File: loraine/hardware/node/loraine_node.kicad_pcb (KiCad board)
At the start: 2 copper layers, 50 x 50 mm, 45 parts, among them CON1 BARREL_JACK, IC1 ATTINY2313A-S, K1 LED1, K2 LED2, K3 LED3, P1 POWER_THRU, P2 POWER, P3 SOLDER_PAD, P4 BUS, P5 BUS_THRU, P6 ICSP, P7 OUTPUTS, Q1 TSM3460CX6, Q2 TSM3460CX6, Q3 TSM3460CX6, Q4 TSM3460CX6, Q5 TSM3460CX6, Q6 TSM3460CX6, Q7 TSM3460CX6, Q8 TSM3460CX6, U1 UA7805CKCT, U2 SN65176BD, X1 16MHz

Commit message: Finished both PCBs apart from logos and checking
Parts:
- C1, C2: value 16p -> 16pF
- C4, C6: value 0.1u -> 0.1uF
- moved P6 45.3 mm to (108.6, 130.7)
- moved C6 15.6 mm to (126.2, 115.6), turned to 0 degrees
- moved C4 8.89 mm to (110.5, 136.4), turned to 270 degrees
- moved K2 6.15 mm to (144.4, 105.0)
- moved P7 2.61 mm to (144.9, 128.9)
- moved U1 2.54 mm to (105.4, 122.6)
- moved U2 2.37 mm to (104.4, 137.2), turned to 270 degrees
- moved C3 2.29 mm to (109.0, 125.0)
- moved C5 2.29 mm to (109.0, 120.1)
- moved R9 1.35 mm to (144.4, 146.4)
- moved R1 1.35 mm to (146.9, 146.4)
- moved Q1 1.09 mm to (145.7, 142.2), turned to 180 degrees
- moved C2 0.65 mm to (120.7, 132.8), turned to 0 degrees
- moved X1 0.46 mm to (118.4, 136.9)
- moved C1 0.18 mm to (116.3, 132.8), turned to 180 degrees
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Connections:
- C3 pad 1: +12V -> VIN
- CON1 pad 1: +12V -> VIN
- K1 pad 3: +5V -> VIN
- K2 pad 3: +5V -> VIN
- K3 pad 3: +5V -> VIN
- P1 pad 2: +12V -> VIN
- P2 pad 2: +12V -> VIN
- P3 pad 2: +12V -> VIN
- P7 pad 1: +12V -> VIN
- P7 pad 11: +12V -> VIN
- P7 pad 13: +12V -> VIN
- P7 pad 15: +12V -> VIN
- P7 pad 3: +12V -> VIN
- P7 pad 5: +12V -> VIN
- P7 pad 7: +12V -> VIN
- P7 pad 9: +12V -> VIN
- U1 pad 2: +12V -> VIN
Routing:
- net GND: track 0.00 -> 302.1 mm, vias 0 -> 14
- net VIN: track 0.00 -> 176.9 mm
- net Net-(IC1-Pad13): track 0.00 -> 128.9 mm, vias 0 -> 3
- net +5V: track 0.00 -> 60.8 mm, vias 0 -> 2
- net Net-(IC1-Pad14): track 0.00 -> 55.0 mm, vias 0 -> 2
- net Net-(IC1-Pad12): track 0.00 -> 49.4 mm, vias 0 -> 1
- net /SCK: track 0.00 -> 43.5 mm, vias 0 -> 1
- net Net-(IC1-Pad2): track 0.00 -> 37.4 mm, vias 0 -> 2
- net /MISO: track 0.00 -> 36.5 mm, vias 0 -> 1
- net /MOSI: track 0.00 -> 30.7 mm, vias 0 -> 1
- net Net-(P4-Pad2): track 0.00 -> 23.6 mm
- net Net-(C2-Pad1): track 0.00 -> 17.9 mm
- net Net-(IC1-Pad15): track 0.00 -> 17.8 mm
- net /RESET: track 0.00 -> 17.7 mm
- net Net-(C1-Pad1): track 0.00 -> 17.6 mm
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- added copper zone on B.Cu, net GND
- added copper zone on F.Cu, net GND

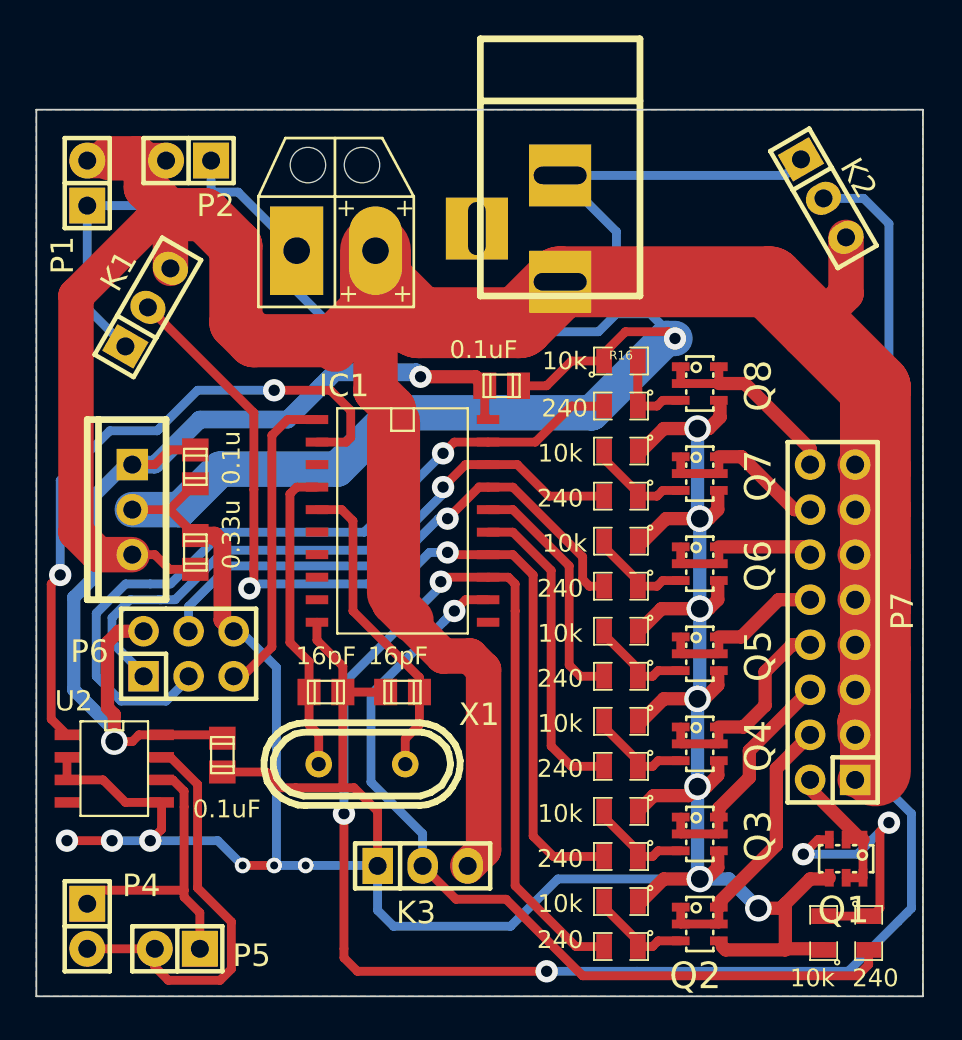
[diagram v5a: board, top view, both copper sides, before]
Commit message: 5V power conn on uplighter board
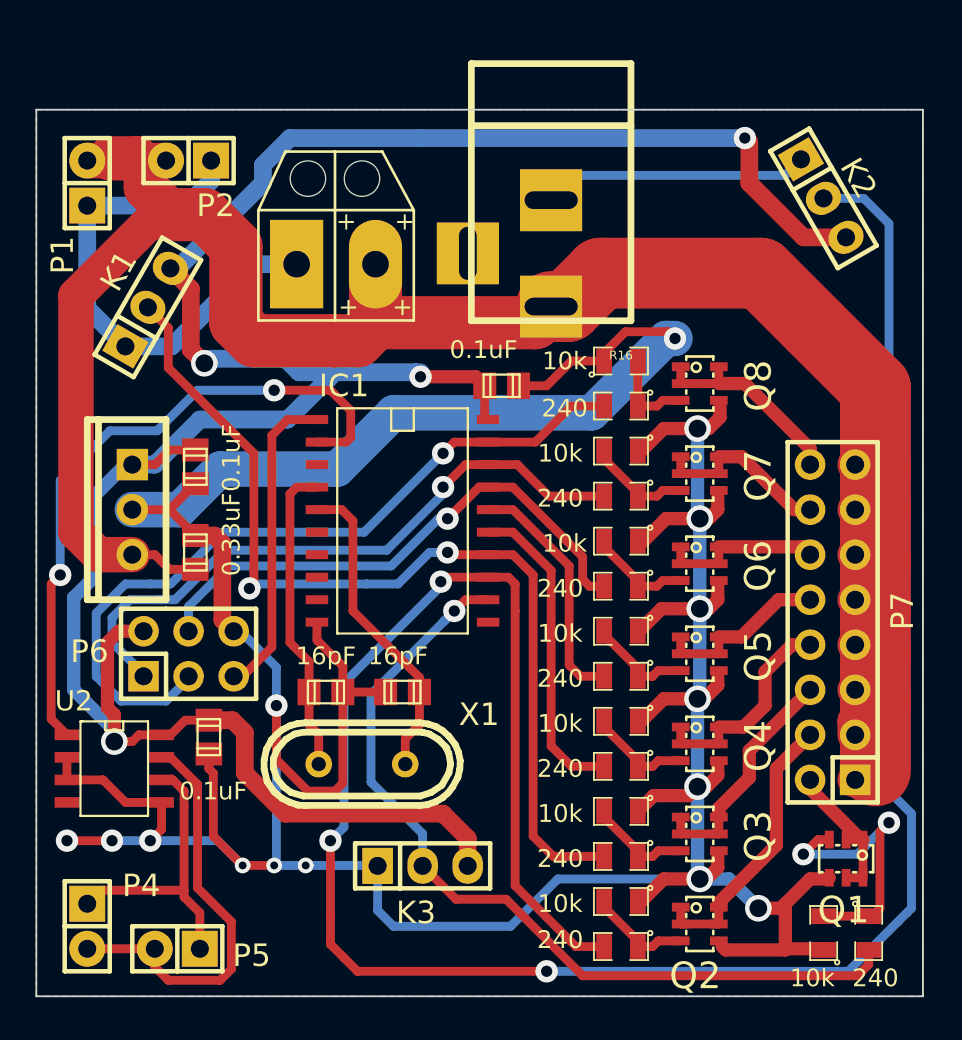
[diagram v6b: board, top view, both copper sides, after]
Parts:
- C3: value 0.33u -> 0.33uF
- C5: value 0.1u -> 0.1uF
- moved CON1 1.49 mm to (129.0, 104.9)
- moved C4 1.27 mm to (109.7, 135.4)
- moved P3 0.76 mm to (116.8, 108.7)
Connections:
- K1 pad 3: VIN -> +5V
- K2 pad 3: VIN -> +5V
- K3 pad 3: VIN -> +5V
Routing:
- net +5V: track 60.8 -> 140.1 mm, vias 2 -> 4
- net VIN: track 176.9 -> 125.9 mm
- net GND: track 302.1 -> 276.5 mm, vias 14 -> 15
- net Net-(IC1-Pad13): track 128.9 -> 129.6 mm

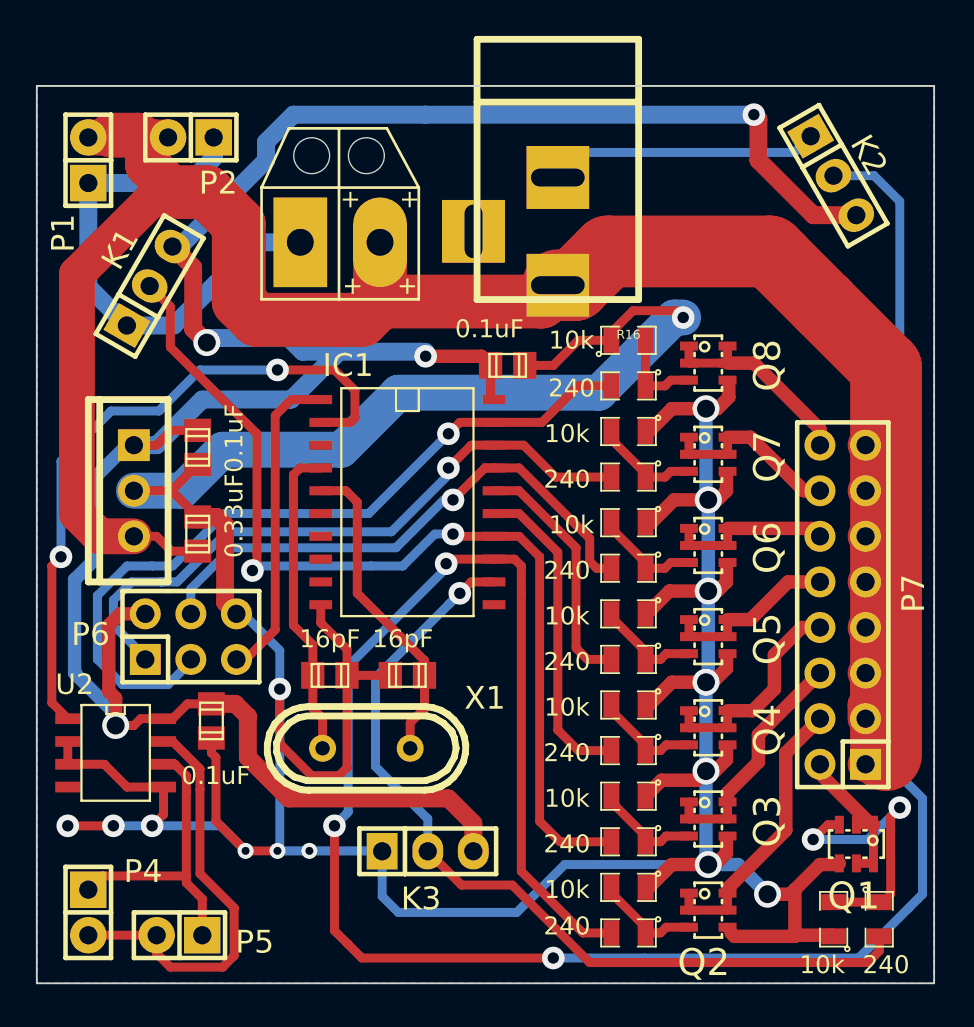
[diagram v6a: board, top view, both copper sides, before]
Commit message: Derouted, chunkified PTH pads
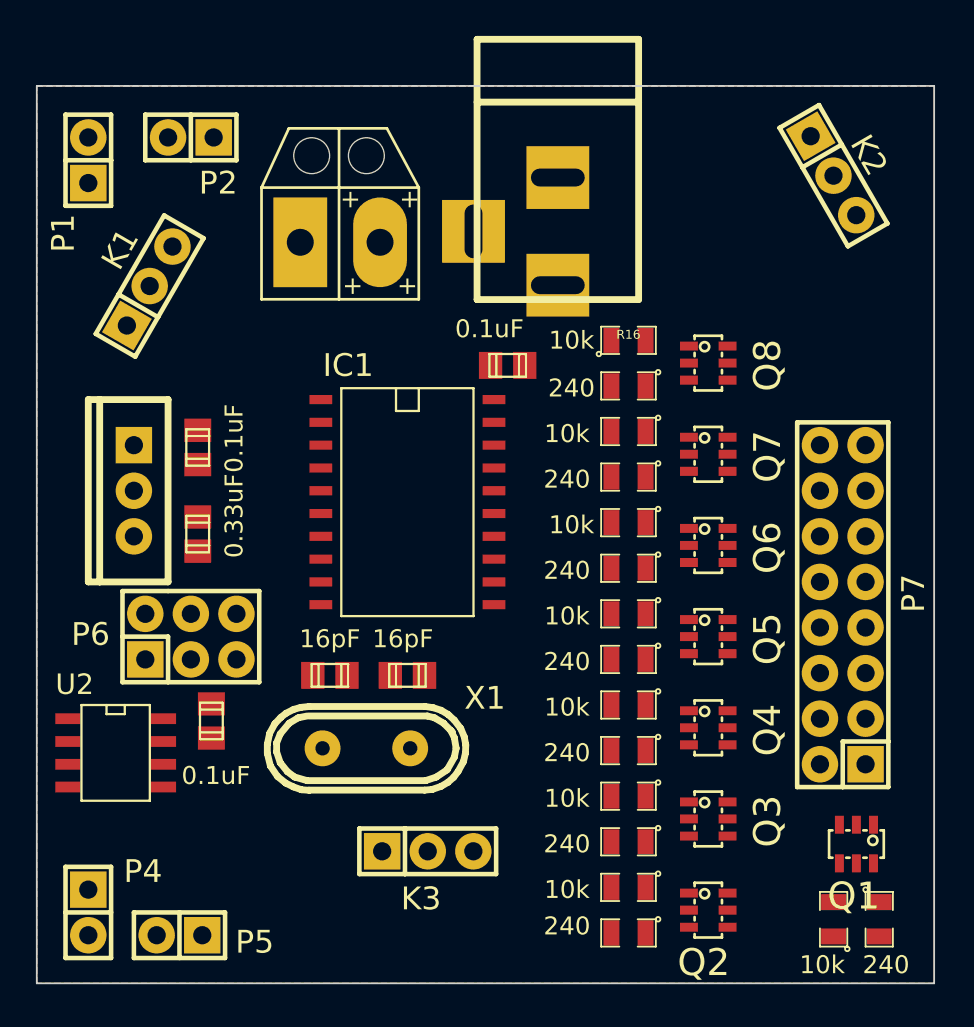
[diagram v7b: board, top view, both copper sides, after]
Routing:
- net GND: track 276.5 -> 0.00 mm, vias 15 -> 0
- net +5V: track 140.1 -> 0.00 mm, vias 4 -> 0
- net Net-(IC1-Pad13): track 129.6 -> 0.00 mm, vias 3 -> 0
- net VIN: track 125.9 -> 0.00 mm
- net Net-(IC1-Pad14): track 55.0 -> 0.00 mm, vias 2 -> 0
- net Net-(IC1-Pad12): track 49.4 -> 0.00 mm, vias 1 -> 0
- net /SCK: track 43.5 -> 0.00 mm, vias 1 -> 0
- net Net-(IC1-Pad2): track 37.4 -> 0.00 mm, vias 2 -> 0
- net /MISO: track 36.5 -> 0.00 mm, vias 1 -> 0
- net /MOSI: track 30.7 -> 0.00 mm, vias 1 -> 0
- net Net-(P4-Pad2): track 23.6 -> 0.00 mm
- net Net-(C2-Pad1): track 17.9 -> 0.00 mm
- net Net-(IC1-Pad15): track 17.8 -> 0.00 mm
- net /RESET: track 17.7 -> 0.00 mm
- net Net-(C1-Pad1): track 17.6 -> 0.00 mm
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
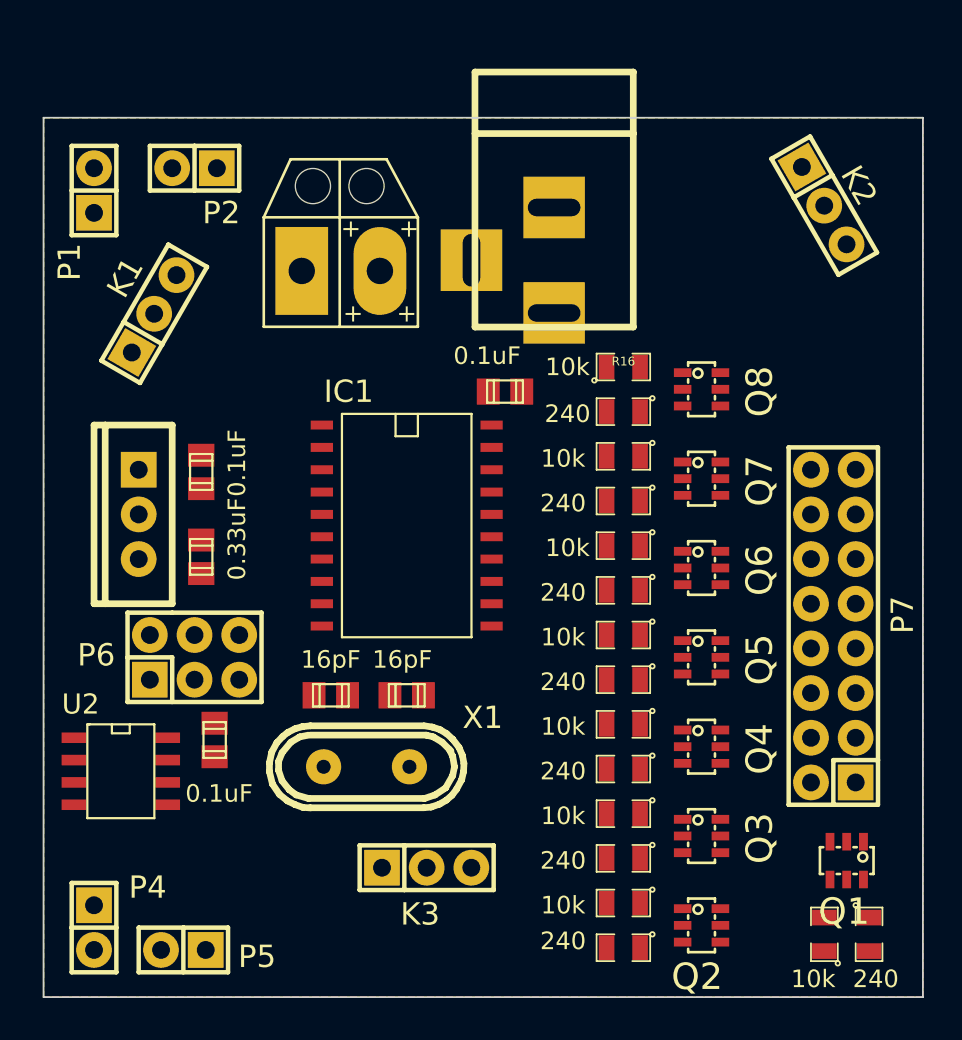
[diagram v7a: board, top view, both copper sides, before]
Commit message: Rerouted loraine node board -- much nicer!
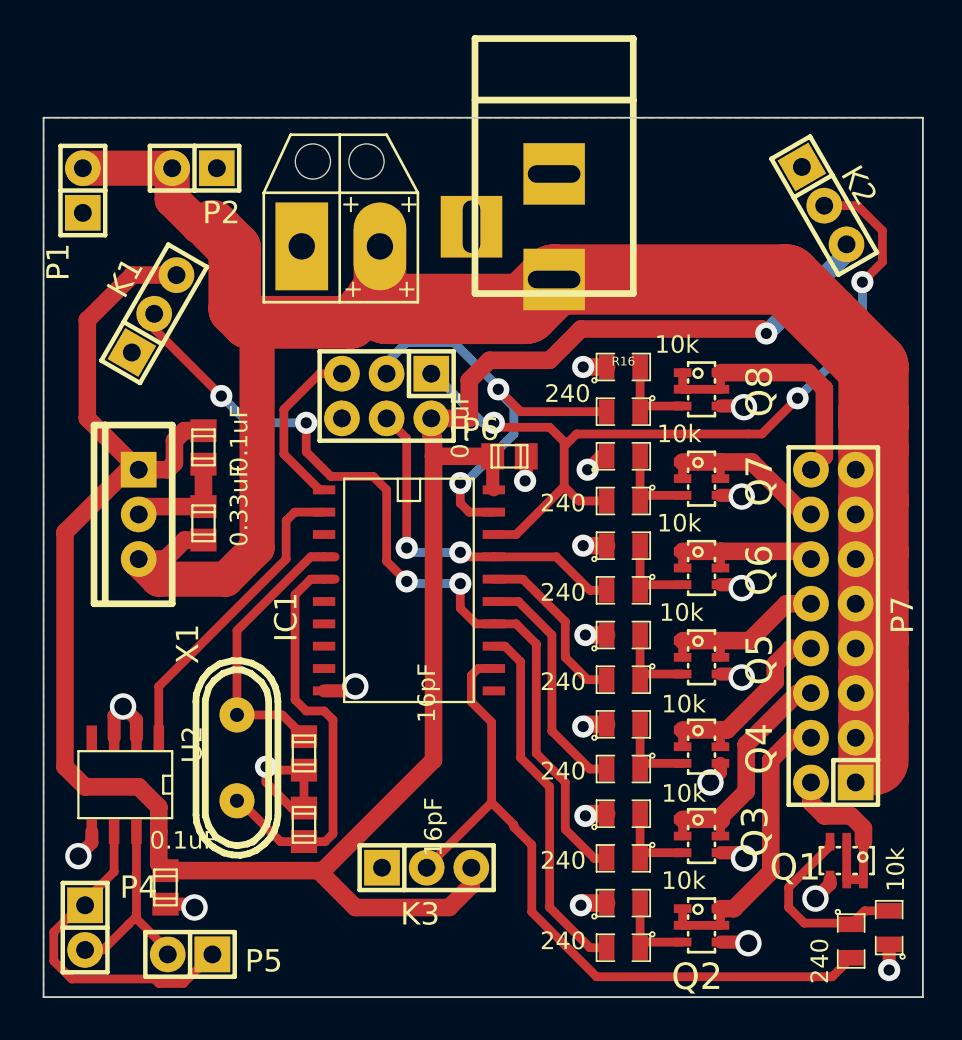
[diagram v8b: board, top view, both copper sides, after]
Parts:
- moved P6 18.4 mm to (119.5, 115.8), turned to 180 degrees
- moved C2 9.40 mm to (114.8, 140.2), turned to 270 degrees
- moved C4 8.84 mm to (106.9, 143.8)
- moved X1 7.38 mm to (111.0, 136.4), turned to 270 degrees
- moved R9 3.70 mm to (148.1, 146.1)
- moved C6 3.69 mm to (126.5, 119.3)
- moved IC1 3.69 mm to (120.8, 126.9)
- moved C1 3.64 mm to (114.8, 136.1), turned to 90 degrees
- moved C3 1.91 mm to (109.1, 123.1)
- moved CON1 1.91 mm to (129.0, 103.0)
- moved C5 1.40 mm to (109.1, 118.7)
- moved P3 1.40 mm to (116.8, 107.3)
- moved R1 1.09 mm to (145.9, 146.8)
- moved U2 0.80 mm to (104.6, 137.9), turned to 180 degrees
- moved P1 0.64 mm to (102.2, 104.1)
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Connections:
- K2 pad 2: Net-(IC1-Pad13) -> /MISO
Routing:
- net +5V: track 0.00 -> 134.7 mm, vias 0 -> 1
- net VIN: track 0.00 -> 118.7 mm
- net /MISO: track 0.00 -> 49.6 mm, vias 0 -> 3
- net Net-(IC1-Pad14): track 0.00 -> 48.5 mm, vias 0 -> 4
- net GND: track 0.00 -> 47.1 mm, vias 0 -> 22
- net Net-(IC1-Pad12): track 0.00 -> 41.7 mm
- net /SCK: track 0.00 -> 26.1 mm, vias 0 -> 2
- net Net-(C2-Pad1): track 0.00 -> 24.3 mm
- net Net-(IC1-Pad13): track 0.00 -> 20.7 mm
- net /MOSI: track 0.00 -> 20.6 mm, vias 0 -> 2
- net Net-(P4-Pad1): track 0.00 -> 19.4 mm
- net Net-(IC1-Pad2): track 0.00 -> 17.7 mm
- net Net-(P7-Pad4): track 0.00 -> 16.9 mm
- net Net-(C1-Pad1): track 0.00 -> 16.4 mm
- net Net-(P7-Pad16): track 0.00 -> 15.3 mm
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- removed copper zone on F.Cu, net GND
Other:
- net class Default: trace_width 0.254 -> 0.5; via_dia 0.889 -> 1.26
- rule trace_min: 0.254 -> 0.5
- rule via_min_size: 0.889 -> 1.26
